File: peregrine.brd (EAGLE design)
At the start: 55.9 x 63.5 mm, 67 parts, among them IC2 LMV358IDGKR, J1 USB MICRO, U1 ITG-3200, U2 ADXL345, U4 3.3V, U5 ATMEGA32U4-XUAU, Y1 16MHz KX-7

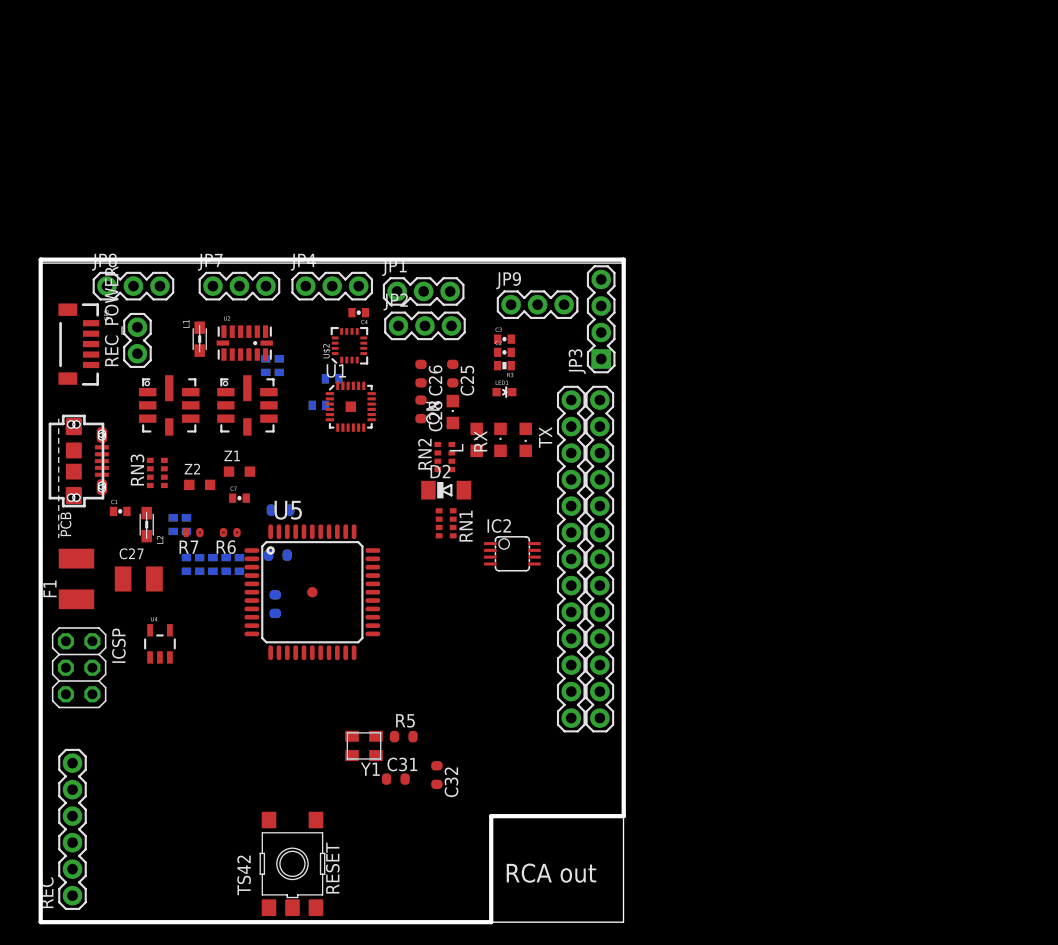
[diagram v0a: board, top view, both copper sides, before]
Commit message: Schematic Changes
Changed a number of nets to reflect desired configuration. Added solder
jumpers for potential "serial dyslexia" resloution. Still needs quite a
few net changes to be completely accurate.
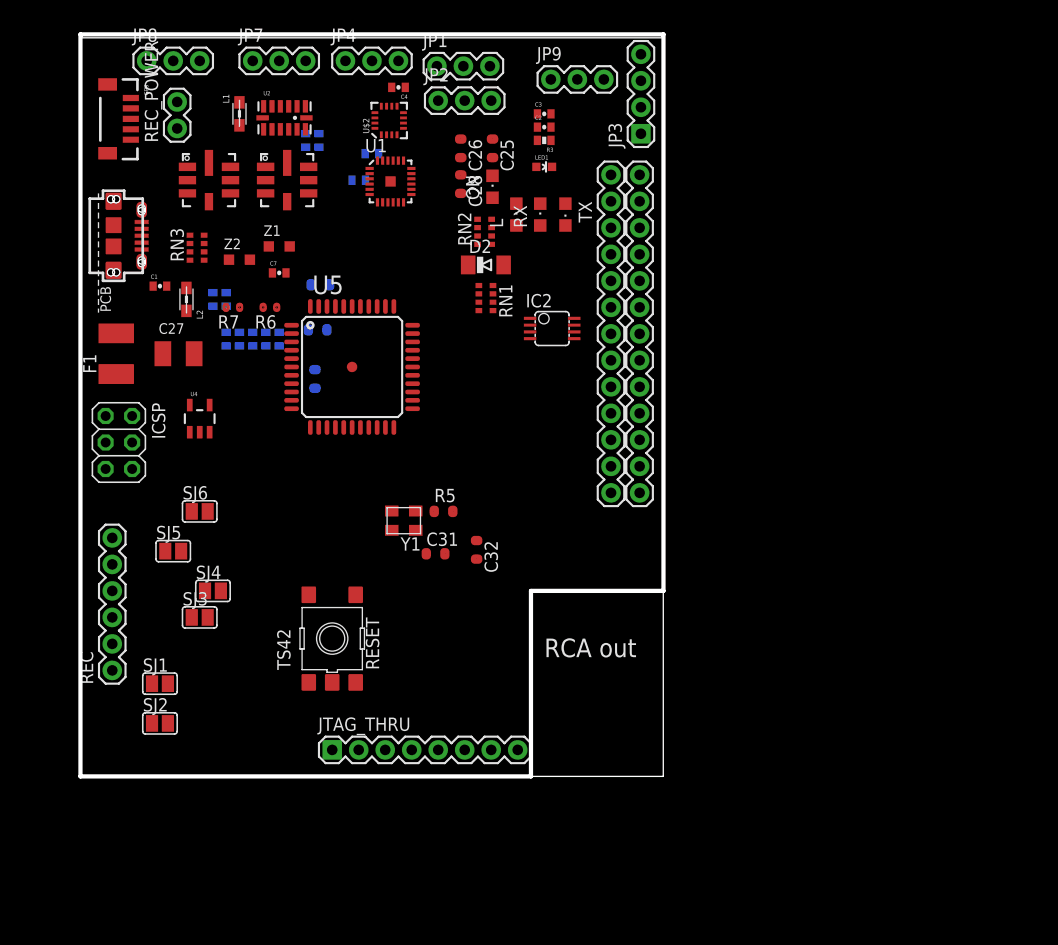
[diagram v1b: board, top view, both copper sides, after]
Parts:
- removed JP5, JP6: M13, SparkFun:1X13
- added BOTTOM, TOP: M13, SparkFun:1X13
- added JTAG_THRU: (no value), SparkFun:1X08
- added SJ1, SJ2, SJ3, SJ4, SJ5, SJ6: (no value), jumper:SJ
- moved C2 21.9 mm to (48.3, 66.0)
- moved C21 21.9 mm to (26.5, 46.6)
- moved C28 21.9 mm to (40.3, 60.6)
- moved C3 21.9 mm to (48.3, 67.3)
- moved C5 21.9 mm to (30.5, 61.0)
- moved C6 21.9 mm to (31.8, 63.5)
- moved GPS 21.9 mm to (8.64, 68.8)
- moved JP1 21.9 mm to (38.0, 71.9)
- moved JP3 21.9 mm to (57.5, 65.4)
- moved JP4 21.9 mm to (29.2, 72.4)
- moved JP7 21.9 mm to (20.3, 72.4)
- moved JP8 21.9 mm to (10.2, 72.4)
- moved L 21.9 mm to (45.6, 57.7)
- moved L1 21.9 mm to (19.1, 67.3)
- moved ON 21.9 mm to (43.3, 60.3)
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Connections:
- removed net COM: GPS.2, REC_POWER.1
- removed net D2/SDA: U5.19
- removed net D3/SCL: U5.18
- removed net VCC: C11.1, JP3.4, U4.1, U4.3
- new net GPIO0(SDA): BOTTOM.2, SJ5.1
- new net GPIO1(SCL): BOTTOM.3, SJ6.1
- new net GPIO10(MOSI): BOTTOM.10
- new net GPIO14(TXD): SJ3.1, TOP.4
- new net GPIO15(RXD): SJ4.1, TOP.5
- new net GPIO17: BOTTOM.6
- new net GPIO18(PCM_CLK): TOP.6
- new net GPIO21(PCM_DOUT): BOTTOM.7
- new net GPIO22: BOTTOM.8
- new net GPIO23: TOP.8
- new net GPIO24: TOP.9
- new net GPIO25: TOP.11
- new net GPIO4(GPCLK0): BOTTOM.4
- new net GPIO7(CE1): TOP.13
- new net GPIO8(CE0): TOP.12
- new net GPIO9(MISO): BOTTOM.11
- new net GPRIO11(SCKL): BOTTOM.12
- new net PI_3V3_1: BOTTOM.1
- new net PI_3V3_2: BOTTOM.9
- new net PI_5V: TOP.1
- new net PI_5V_2: TOP.2
- new net PI_GND1: BOTTOM.5
- new net PI_GND2: BOTTOM.13
- new net PI_GND3: TOP.3
- new net PI_GND4: TOP.7
- new net PI_GND5: TOP.10
- net +5V: now also C11.1, JP3.4, U4.1, U4.3
- net D0/RX: now also SJ2.2, SJ3.2
- net D1/TX: now also SJ1.2, SJ4.2
- net GND: now also GPS.2, REC_POWER.1
- net GPS-RX: now also SJ2.1
- net GPS-TX: now also SJ1.1
- net SCL: now also SJ6.2, U5.18
- net SDA: now also SJ5.2, U5.19
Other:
- board size 55.9 x 63.5 mm -> 55.9 x 71.1 mm

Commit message: Tweaked placement
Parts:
- moved RN3 34.2 mm to (31.5, 24.5), turned to 90 degrees
- moved C32 29.5 mm to (16.9, 9.78), turned to 90 degrees
- moved R5 27.3 mm to (19.8, 9.40)
- moved TX 27.0 mm to (36.3, 34.5), turned to 270 degrees
- moved JP8 26.9 mm to (36.6, 67.2)
- moved IC2 24.9 mm to (26.2, 36.8), turned to 90 degrees
- moved JP7 24.8 mm to (44.6, 67.2)
- moved RX 24.4 mm to (36.3, 36.2), turned to 270 degrees
- moved RN1 24.1 mm to (31.5, 28.3)
- moved RN2 23.9 mm to (30.4, 35.4)
- moved REC_POWER 23.9 mm to (36.6, 70.1), turned to 0 degrees
- moved C31 23.7 mm to (17.5, 13.0)
- moved D2 23.6 mm to (31.5, 32.0)
- moved SJ3 23.6 mm to (37.8, 12.2), turned to 270 degrees
- moved C23 21.9 mm to (11.6, 25.7), flipped to the top, turned to 90 degrees
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
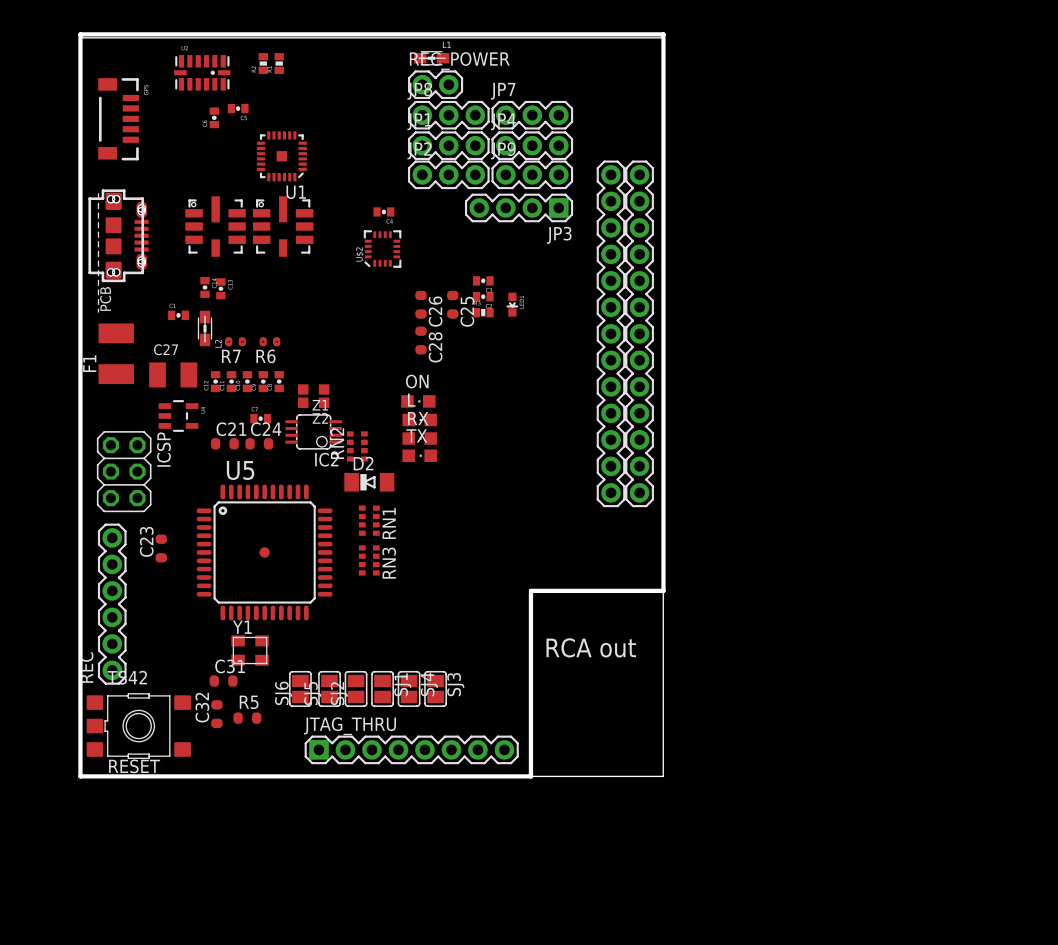
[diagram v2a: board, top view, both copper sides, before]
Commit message: Changed around layout.
Changed a bunch of headers so that they were small perofile or locking.
Ignored RCA plug, just assuming that we can build above it. Added two
standoff holes for support above the board. The standoffs would touch on
blank spots on the pi.
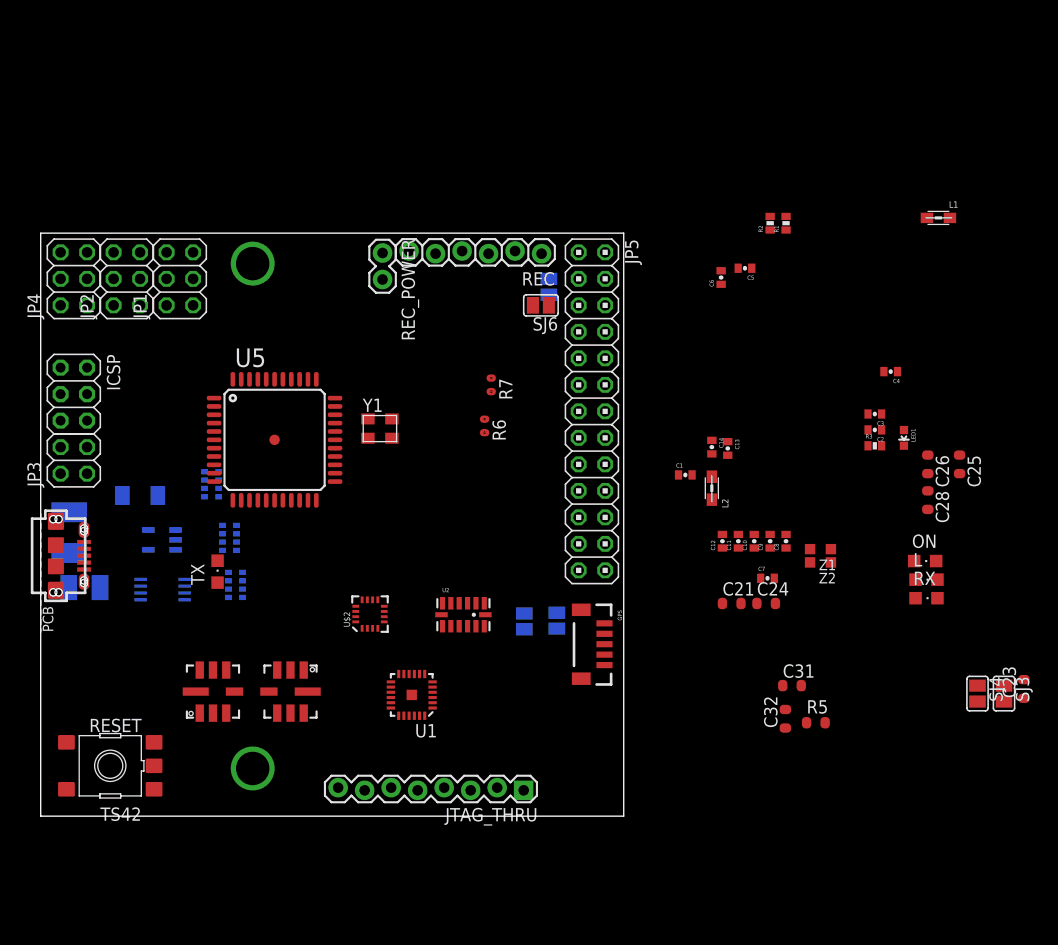
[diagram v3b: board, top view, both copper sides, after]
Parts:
- removed BOTTOM, TOP: M13, SparkFun:1X13
- removed JP7, JP8, JP9: (no value), SparkFun:1X03
- added JP5: (no value), pinhead:2X13
- JP1, JP2, JP4: device SparkFun:1X03 -> pinhead:2X03
- JP3: device SparkFun:1X04 -> pinhead:2X02
- JTAG_THRU: device SparkFun:1X08 -> SparkFun:1X08_LOCK
- REC: device SparkFun:1X06 -> SparkFun:1X06_LOCK
- moved C23 83.8 mm to (94.2, 12.2)
- moved GPS 67.8 mm to (54.0, 18.5)
- moved U2 57.7 mm to (40.5, 19.3)
- moved REC 57.3 mm to (48.0, 53.9), turned to 180 degrees
- moved C31 54.5 mm to (72.0, 12.5)
- moved R5 54.5 mm to (74.3, 8.95)
- moved SJ4 54.5 mm to (89.8, 11.7)
- moved C32 54.5 mm to (71.4, 9.33)
- moved SJ3 54.5 mm to (92.3, 11.7)
- moved U1 53.1 mm to (35.6, 11.6)
- moved JP3 52.4 mm to (3.17, 34.1), turned to 90 degrees
- moved C13 50.9 mm to (65.8, 35.2)
- moved C14 50.9 mm to (64.3, 35.4)
- moved C21 50.9 mm to (66.2, 20.4)
- moved C28 50.9 mm to (85.0, 30.3)
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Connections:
- removed net GPIO18(PCM_CLK): TOP.6
- removed net GPIO23: TOP.8
- removed net GPIO24: TOP.9
- removed net GPIO25: TOP.11
- removed net GPIO7(CE1): TOP.13
- removed net GPIO8(CE0): TOP.12
- removed net PI_5V: TOP.1
- removed net PI_5V_2: TOP.2
- removed net PI_GND3: TOP.3
- removed net PI_GND4: TOP.7
- removed net PI_GND5: TOP.10
- net +5V: now also JP1.3, JP1.4, JP2.3, JP2.4, JP3.2, JP4.3, JP4.4; no longer JP1.2, JP2.2, JP3.4, JP4.2, JP7.2, JP8.2, JP9.2
- net GND: now also JP1.5, JP1.6, JP2.5, JP2.6, JP3.4, JP4.5, JP4.6; no longer JP1.1, JP2.1, JP3.3, JP4.1, JP7.1, JP8.1, JP9.1
- net GPIO0(SDA): now also JP5.3; no longer BOTTOM.2
- net GPIO1(SCL): now also JP5.5; no longer BOTTOM.3
- net GPIO10(MOSI): now also JP5.19; no longer BOTTOM.10
- net GPIO14(TXD): no longer TOP.4
- net GPIO15(RXD): no longer TOP.5
- net GPIO17: now also JP5.11; no longer BOTTOM.6
- net GPIO21(PCM_DOUT): now also JP5.13; no longer BOTTOM.7
- net GPIO22: now also JP5.15; no longer BOTTOM.8
- net GPIO4(GPCLK0): now also JP5.7; no longer BOTTOM.4
- net GPIO9(MISO): now also JP5.21; no longer BOTTOM.11
- net GPRIO11(SCKL): now also JP5.23; no longer BOTTOM.12
- net M_1: now also JP1.2; no longer JP1.3
- net M_2: now also JP2.2; no longer JP2.3
- net M_3: now also JP4.2; no longer JP4.3
- net M_4: now also JP1.1; no longer JP7.3
- net M_AUX1: now also JP4.1; no longer JP9.3
- net M_AUX2: now also JP2.1; no longer JP8.3
- net PI_3V3_1: now also JP5.1; no longer BOTTOM.1
- net PI_3V3_2: now also JP5.17; no longer BOTTOM.9
- net PI_GND1: now also JP5.9; no longer BOTTOM.5
- net PI_GND2: now also JP5.25; no longer BOTTOM.13
- net SCL: now also JP3.3; no longer JP3.1
- net SDA: now also JP3.1; no longer JP3.2
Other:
- board size 55.9 x 71.1 mm -> 55.9 x 55.9 mm
- board text removed: "RCA out"

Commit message: Initial route completed
The other random files are from converting it to a couple different
formats to try some autorouters out.
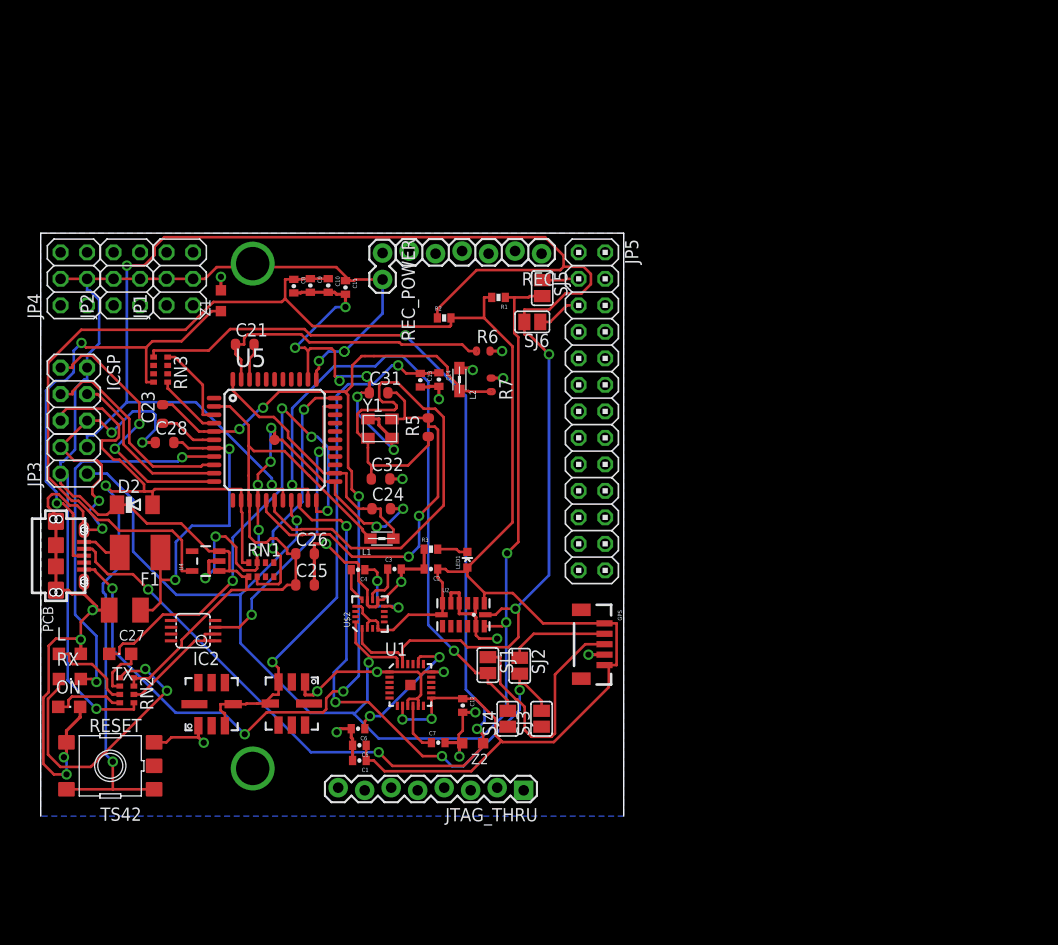
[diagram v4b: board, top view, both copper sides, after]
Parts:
- moved C23 86.7 mm to (11.7, 38.5)
- moved ON 83.2 mm to (2.73, 10.5)
- moved RX 82.5 mm to (2.79, 13.1)
- moved L 82.4 mm to (2.79, 15.6)
- moved C28 73.4 mm to (11.9, 35.8), turned to 0 degrees
- moved C25 63.8 mm to (25.3, 22.2), turned to 0 degrees
- moved Z1 62.2 mm to (17.3, 49.4), turned to 90 degrees
- moved L1 61.6 mm to (32.7, 26.6), turned to 0 degrees
- moved C26 60.3 mm to (25.3, 25.1), turned to 0 degrees
- moved C5 58.8 mm to (30.5, 6.79)
- moved C6 55.5 mm to (30.4, 8.38), turned to 180 degrees
- moved C4 54.5 mm to (30.4, 23.6)
- moved C8 53.1 mm to (24.3, 50.8), turned to 270 degrees
- moved C21 52.9 mm to (19.6, 45.2)
- moved C9 50.4 mm to (25.8, 50.9), turned to 270 degrees
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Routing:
- net GND: track 0.00 -> 257.2 mm, vias 0 -> 41
- net 3V3: track 0.00 -> 200.1 mm, vias 0 -> 2
- net +5V: track 0.00 -> 181.3 mm, vias 0 -> 4
- net SCL: track 0.00 -> 167.7 mm, vias 0 -> 4
- net SDA: track 0.00 -> 128.4 mm, vias 0 -> 4
- net D-: track 0.00 -> 117.2 mm, vias 0 -> 4
- net UGND: track 0.00 -> 106.1 mm, vias 0 -> 6
- net RESET: track 0.00 -> 78.2 mm, vias 0 -> 2
- net D1/TX: track 0.00 -> 61.8 mm, vias 0 -> 2
- net XTAL1: track 0.00 -> 58.4 mm
- net D0/RX: track 0.00 -> 53.0 mm, vias 0 -> 4
- net 3.3V: track 0.00 -> 51.7 mm, vias 0 -> 2
- net TXLED: track 0.00 -> 47.9 mm, vias 0 -> 4
- net D+: track 0.00 -> 43.8 mm, vias 0 -> 2
- net XTAL2: track 0.00 -> 38.9 mm, vias 0 -> 2
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- added copper zone on layer 16, net GND
